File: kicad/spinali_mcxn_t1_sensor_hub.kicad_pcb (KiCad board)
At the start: 4 copper layers, 186 parts, among them J1 5055780421, J2 USB4105-GF-A, J3 CAN0A, J4 CAN0B, J6 CAN1A, J7 CAN1B, J8 DF40TC-50DP-0.4V(51), J9 DF40TC-50DP-0.4V(51), Q1 BUK6D56-60EX, SW1 SW_SPST, U1 LM74700, U10 BMM350, U11 BMP581, U12 TJA1462ATK, U13 TJA1462ATK, U14 SK9822-EC20, U15 TJA1103AHN, U2 NX5P3363UKZ, U3 LM5160DNTJ, U4 NX5P3363UKZ, U5 MIC5504-1.8YMT, U6 MPM3811GG-Z, U7 MCXN947VDFT, U8 PCMF1USB3SZ, U9 ICM-45686, Y1 24MHz, Y2 32.768kHz, Y3 25MHz

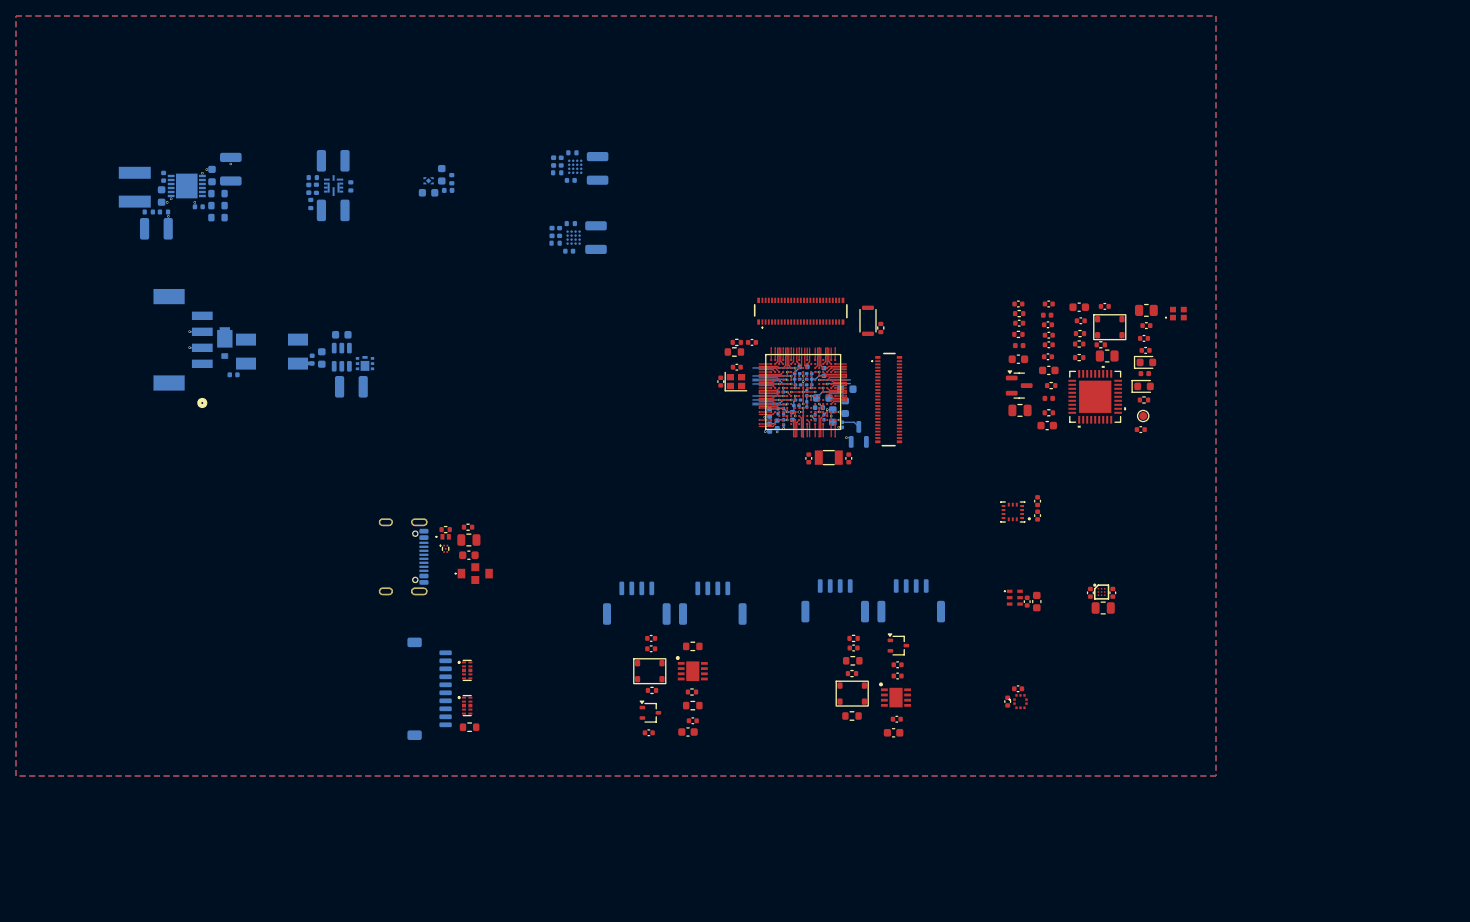
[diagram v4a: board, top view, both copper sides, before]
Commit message: Updated schematic after feedback from Jari
- Finished schematic after feedback from Jari. It is at a finished state, can be reviewed by whole team now.
- Layouted MCXN with decoupling caps.
- Layouted Base100-T1 ethernet phy.
- Layouted the power supply a bit.
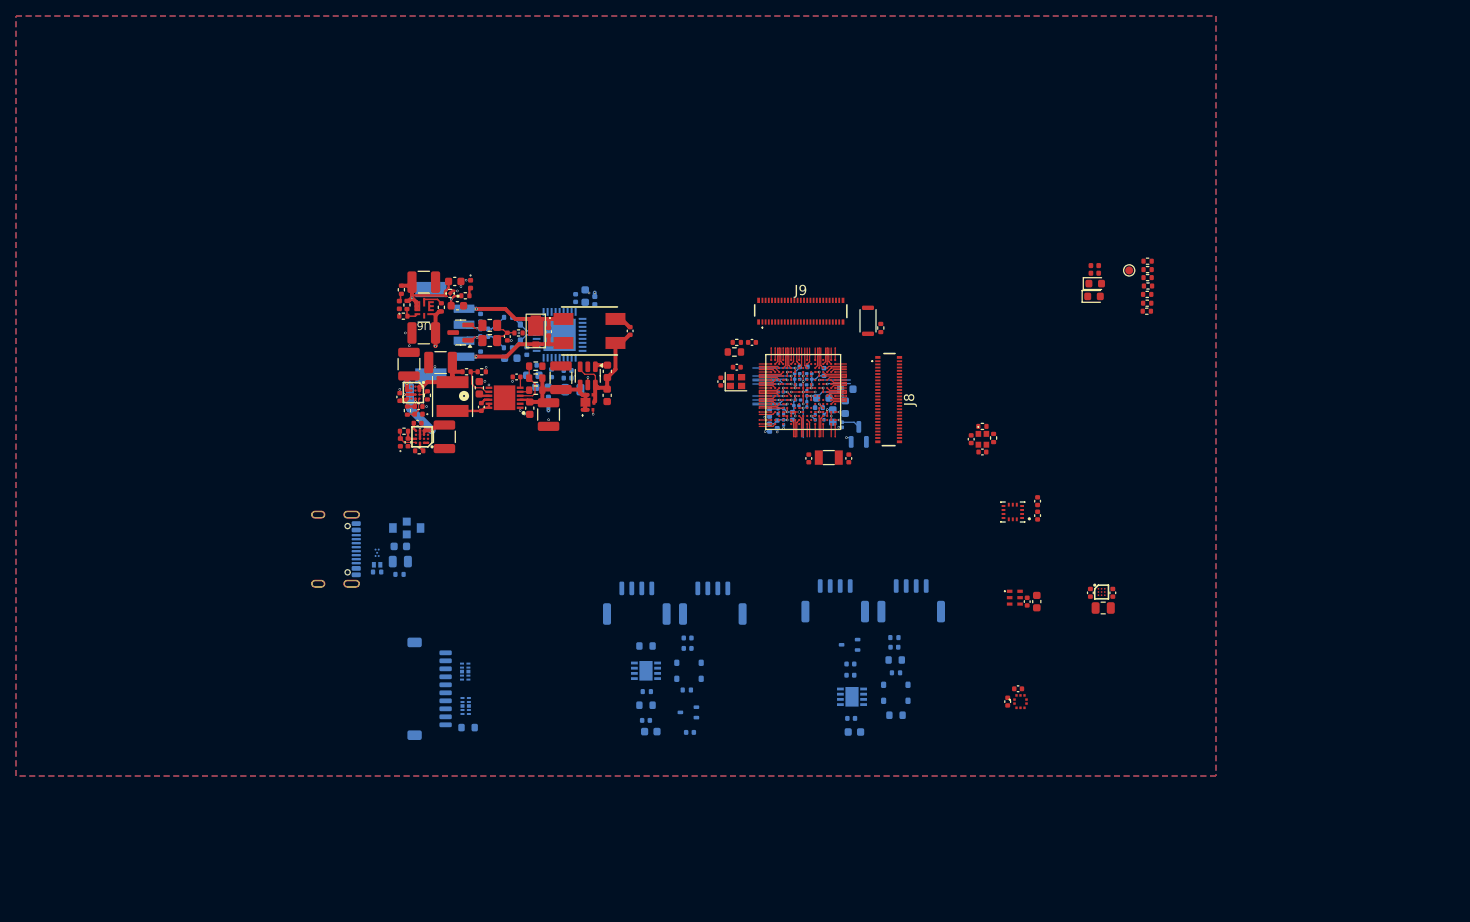
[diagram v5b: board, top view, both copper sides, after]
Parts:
- added R42: 15, Resistor_SMD:R_0402_1005Metric, F.Cu at (155.8, 101.3)
- added R43: 15, Resistor_SMD:R_0402_1005Metric, F.Cu at (157.2, 102.8)
- added R44: 100k 1/10W, Resistor_SMD:R_0402_1005Metric, F.Cu at (97.8, 89.6)
- C1, C10, C11, C12, C13, C14, C15, C16, C17, C18, C19, C2, C20, C21, C3, C4, C5, C6, C7, C8, C9, D2, D3, D4, D5, L1, L2, Q1, R1, R10, R11, R12, R13, R14, R2, R3, R4, R5, R6, R7, R8, R9, U1, U2, U3, U4, U5, U6: moved to F.Cu
- C53, C54, C55, C63, C64, C65, C66, C67, C68, C69, C70, C71, C72, C75, C76, C77, C78, C79, C80, C81, C82, C83, C84, C85, C86, C87, C89, C90, D10, D11, D15, D8, D9, L5, L6, L7, L8, L9, R18, R19, R20, R21, R22, R23, R24, R25, R26, R27, R28, R35, R38, U12, U13, U15, U8: moved to B.Cu
- C91, C92: value 8pF 16V -> 10pF 16V
- D1: value 6DFN62CA-M3/I -> 6DFN56CA-M3/I; moved to F.Cu
- J5: value ~ -> Debug
- J8, J9: value DF40TC-50DP-0.4V(51) -> DF40TC(3.0)-50DP-0.4V(51); footprint Connectors:DF40TC-50DP-0.4V(51) -> Connectors:DF40TC(3.0)-50DP-0.4V(51)
- moved C87 83.1 mm to (93.1, 91.5), turned to 90 degrees
- moved C90 82.8 mm to (93.5, 89.1), turned to 180 degrees
- moved C86 82.5 mm to (93.5, 90.1), turned to 180 degrees
- moved R36 82.1 mm to (94.2, 88.7)
- moved C89 78.0 mm to (93.1, 87.7), turned to 90 degrees
- moved R37 77.2 mm to (94.2, 90.6)
- moved R38 74.2 mm to (96.5, 87.7)
- moved L9 72.2 mm to (98.0, 88.6), turned to 180 degrees
- moved D14 70.1 mm to (90.6, 89.6), turned to 180 degrees
- moved C85 68.8 mm to (99.6, 94.9)
- moved R35 68.1 mm to (96.5, 91.5), turned to 180 degrees
- moved C88 67.6 mm to (96.4, 90.1), turned to -90 degrees
- moved C84 67.6 mm to (96.8, 92.8)
- moved U15 67.4 mm to (103.0, 89.9), turned to 90 degrees
- moved C83 65.3 mm to (98.8, 91.9), turned to 90 degrees
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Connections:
- net /Ethernet PHY/TRX_M renamed /Ethernet PHY/TRX_N
- C1 pad 2: GND -> Net-(C1-Pad2)
- C88 pad 1: GND -> Net-(C88-Pad1)
- C88 pad 2: Net-(C88-Pad2) -> GND
- C89 pad 1: ENET0_TRX_M -> ENET0_TRX_N
- C90 pad 2: ENET0_TRX_M -> ENET0_TRX_N
- C91 pad 1: /Ethernet PHY/ENET0_XTAL_IN -> Net-(C91-Pad1)
- C92 pad 1: /Ethernet PHY/ENET0_XTAL_OUT -> Net-(C92-Pad1)
- D1 pad 1: GND -> Net-(C1-Pad2)
- D14 pad 2: ENET0_TRX_M -> ENET0_TRX_N
- J1 pad 3: ENET0_TRX_M -> ENET0_TRX_N
- J1 pad 4: GND -> Net-(C1-Pad2)
- L1 pad 1: Net-(C1-Pad1) -> Net-(C1-Pad2)
- L1 pad 2: GND -> Net-(C1-Pad1)
- L1 pad 3: GND -> Net-(Q1-S)
- L1 pad 4: Net-(Q1-S) -> GND
- R36 pad 1: ENET0_TRX_P -> ENET0_TRX_N
- R36 pad 2: Net-(C88-Pad2) -> Net-(C88-Pad1)
- R37 pad 1: Net-(C88-Pad2) -> ENET0_TRX_P
- R37 pad 2: ENET0_TRX_M -> Net-(C88-Pad1)
- Y3 pad 1: /Ethernet PHY/ENET0_XTAL_IN -> Net-(C92-Pad1)
- Y3 pad 3: /Ethernet PHY/ENET0_XTAL_OUT -> Net-(C91-Pad1)
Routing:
- net +5V: track 0.00 -> 26.6 mm, vias 0 -> 3
- net +3V3: track 56.2 -> 35.5 mm, vias 8 -> 11
- net +BATT: track 0.00 -> 17.4 mm
- net Net-(Q1-S): track 1.78 -> 16.1 mm
- net Net-(C1-Pad1): track 0.00 -> 14.2 mm, vias 0 -> 1
- net Net-(U4-EN): track 0.00 -> 14.2 mm, vias 0 -> 2
- net Net-(C1-Pad2): track 0.00 -> 14.1 mm, vias 0 -> 1
- net Net-(U7H-VDD_CORE_1): track 17.1 -> 9.46 mm
- net GND: track 18.0 -> 25.1 mm, vias 26 -> 39
- net Net-(Q1-G): track 0.00 -> 6.39 mm, vias 0 -> 2
- net Net-(U3-EN/UVLO): track 0.00 -> 5.67 mm
- net ENET0_TRX_N: track 0.00 -> 5.28 mm, vias 0 -> 1
- net Net-(C9-Pad2): track 0.00 -> 5.22 mm
- net Net-(U3-FB): track 0.00 -> 5.00 mm
- net Net-(C88-Pad1): track 0.00 -> 4.77 mm
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- added copper zone on In3.Cu, net +3V3
- added copper zone on In2.Cu, net GND
- added copper zone on In4.Cu, net GND
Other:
- copper layers 4 -> 6

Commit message: Finished schematic. Completed power and ENET phy layout.
Layouted power supply and ethernet phy around input connector.
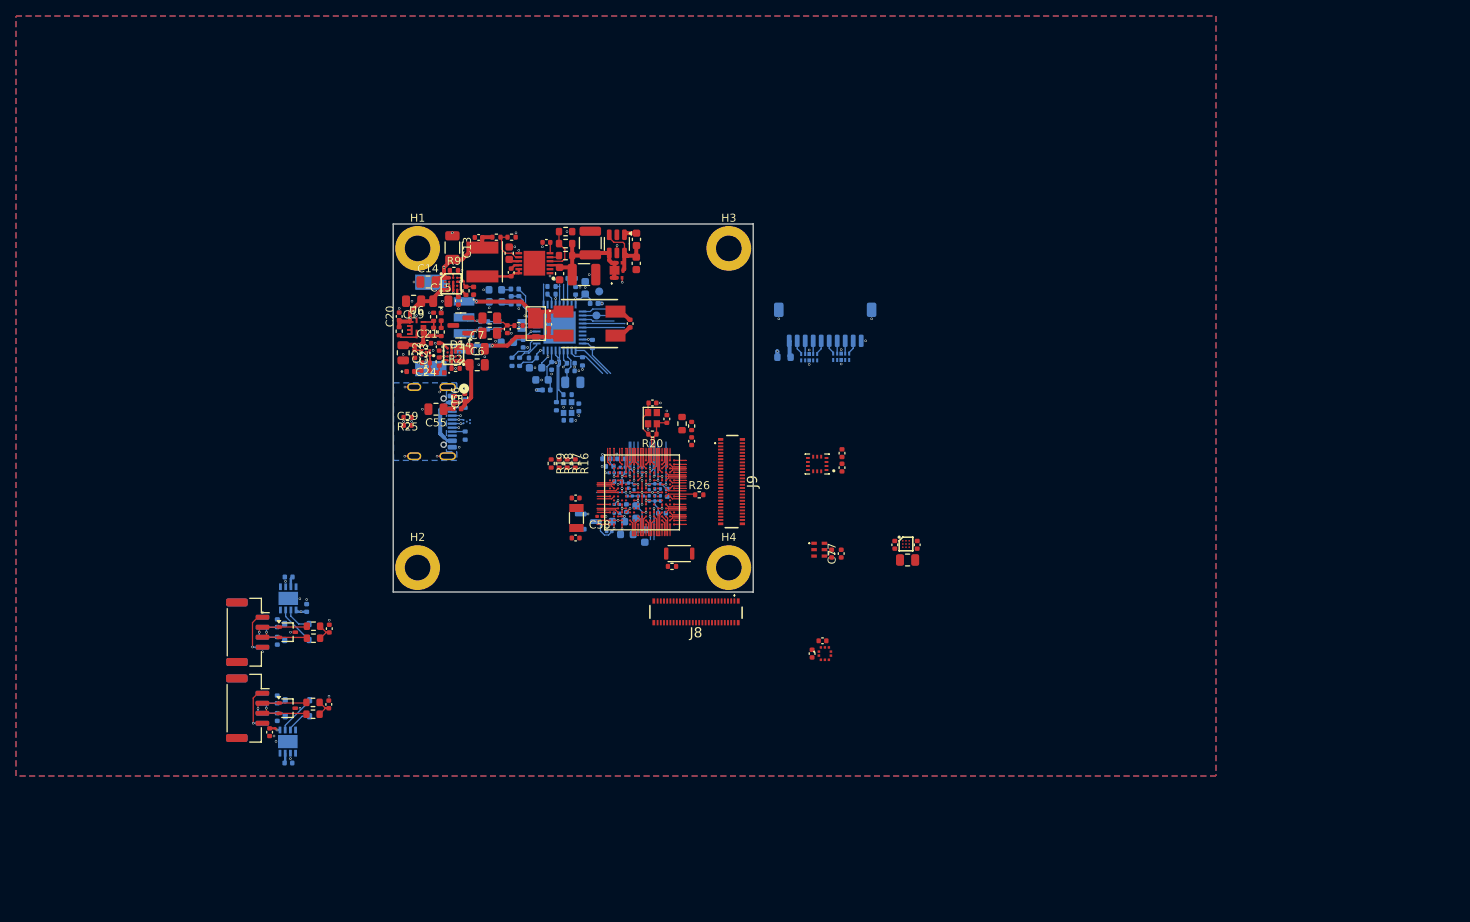
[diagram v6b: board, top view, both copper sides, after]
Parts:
- removed the C12 at (88.1, 93.3)
- removed the C16 at (86.0, 83.3)
- removed the C46 at (137.1, 100.0)
- removed the C53 at (83.8, 114.0)
- removed the C54 at (83.0, 118.2)
- removed the C65 at (139.3, 131.0)
- removed the C67 at (139.3, 132.4)
- removed the C70 at (119.0, 129.1)
- removed the C72 at (119.0, 127.8)
- removed the C87 at (93.1, 91.5)
- removed the C89 at (93.1, 87.7)
- removed the L9 at (98.0, 88.6)
- removed the R14 at (86.4, 97.4)
- removed the R23 at (144.8, 127.7)
- removed the R28 at (113.8, 134.4)
- removed the R35 at (96.5, 91.5)
- removed the R38 at (96.5, 87.7)
- added C13: 22uF 10V, Capacitor_SMD:C_1206_3216Metric, F.Cu at (89.5, 79.0)
- added C19: 10uF 10V, Capacitor_SMD:C_0805_2012Metric, F.Cu at (84.7, 85.7)
- added C20: 100nF 16V, Capacitor_SMD:C_0402_1005Metric, F.Cu at (82.9, 87.5)
- added C21: 100nF 16V, Capacitor_SMD:C_0402_1005Metric, F.Cu at (86.4, 90.9)
- added C22: 10uF 10V, Capacitor_SMD:C_0805_2012Metric, F.Cu at (83.4, 92.1)
- added C49: 10uF 6.3V, Capacitor_SMD:C_0603_1608Metric, B.Cu at (110.3, 113.2)
- added C55: 1uF 50V, Capacitor_SMD:C_0805_2012Metric, F.Cu at (87.5, 99.2)
- added C58: 100nF 10V, Capacitor_SMD:C_0201_0603Metric, F.Cu at (108.0, 112.5)
- added C59: 10nF 16V, Capacitor_SMD:C_0402_1005Metric, F.Cu at (84.0, 101.2)
- added C69: 56pF 10V, Capacitor_SMD:C_0402_1005Metric, B.Cu at (67.7, 137.6)
- added C71: 56pF 10V, Capacitor_SMD:C_0402_1005Metric, B.Cu at (67.7, 135.4)
- added C74: 56pF 10V, Capacitor_SMD:C_0402_1005Metric, B.Cu at (67.7, 128.1)
- added C76: 56pF 10V, Capacitor_SMD:C_0402_1005Metric, B.Cu at (67.7, 125.9)
- added H1: MountingHole, MountingHole:MountingHole_3.2mm_M3_DIN965_Pad, F.Cu at (85.2, 79.0)
- added H2: MountingHole, MountingHole:MountingHole_3.2mm_M3_DIN965_Pad, F.Cu at (85.2, 119.0)
- added H3: MountingHole, MountingHole:MountingHole_3.2mm_M3_DIN965_Pad, F.Cu at (124.1, 79.0)
- added H4: MountingHole, MountingHole:MountingHole_3.2mm_M3_DIN965_Pad, F.Cu at (124.1, 119.0)
- added L10: ACT1210L-201-2P-TL00, Inductors:ACT1210L1012PTL00, B.Cu at (96.7, 88.7)
- added L5: 600 Ohm, Inductor_SMD:L_0402_1005Metric, F.Cu at (90.2, 99.1)
- added R16: 10k, Resistor_SMD:R_0402_1005Metric, F.Cu at (104.9, 105.9)
- added R17: 10k, Resistor_SMD:R_0402_1005Metric, F.Cu at (103.9, 105.9)
- added R18: 10k, Resistor_SMD:R_0402_1005Metric, F.Cu at (102.9, 105.9)
- added R19: 10k, Resistor_SMD:R_0402_1005Metric, F.Cu at (101.9, 105.9)
- added R26: 0R, Resistor_SMD:R_0402_1005Metric, F.Cu at (120.4, 109.8)
- added R36: 10k, Resistor_SMD:R_0402_1005Metric, B.Cu at (97.8, 85.5)
- added R9: 30k 1%, Resistor_SMD:R_0402_1005Metric, F.Cu at (89.7, 81.8)
- added TP2: GND, TestPoint:TestPoint_Pad_D1.0mm, B.Cu at (107.9, 84.4)
- C14, C15: value 47uF 16V -> 10uF 10V; footprint Capacitor_SMD:C_1210_3225Metric -> Capacitor_SMD:C_0805_2012Metric
- C16: renamed from C19; value 22nF 10V -> 22nF 16V
- C23: renamed from C17; footprint Capacitor_SMD:C_0603_1608Metric -> Capacitor_SMD:C_0402_1005Metric
- C24: renamed from C18; footprint Capacitor_SMD:C_0603_1608Metric -> Capacitor_SMD:C_0402_1005Metric
- C56: renamed from C55; footprint Capacitor_SMD:C_0603_1608Metric -> Capacitor_SMD:C_0402_1005Metric; moved to F.Cu
- C6: value 100nF 16V -> 10uF 10V; footprint Capacitor_SMD:C_0402_1005Metric -> Capacitor_SMD:C_0805_2012Metric
- C67: renamed from C63; moved to F.Cu
- C68: renamed from C64; footprint Capacitor_SMD:C_0603_1608Metric -> Capacitor_SMD:C_0402_1005Metric
- C7: value 47uF 16V -> 10uF 16V; footprint Capacitor_SMD:C_1210_3225Metric -> Capacitor_SMD:C_0805_2012Metric
- C70: renamed from C66; moved to F.Cu
- C73: renamed from C69; footprint Capacitor_SMD:C_0603_1608Metric -> Capacitor_SMD:C_0402_1005Metric
- C75: renamed from C71; moved to F.Cu
- C77: renamed from C73; footprint Capacitor_SMD:C_0603_1608Metric -> Capacitor_SMD:C_0402_1005Metric
- C9: value 10nF 16V -> 10nF 25V
- C90: renamed from C91; moved to B.Cu
- C91: renamed from C92; moved to B.Cu
- D10, D11, J4, J7: moved to F.Cu
- D12, D13, R39, TP1, Y3: moved to B.Cu
- D14: value VETH100A203S-G3-18 -> PESD2ETH1G-T
- D7: renamed from D15; moved to F.Cu
- L2: value 33uH 1.3A -> 22uH 1.8A
- R2: value 24k 1% -> 30k 1%
- R20: value 0 -> 1M; moved to F.Cu
- R25: value 0 -> 0R; moved to F.Cu
- R27: renamed from R21; moved to F.Cu
- R28: renamed from R22; moved to F.Cu
- R3: value 100k 75V -> 100k 1% 75V
- R30: renamed from R26; moved to F.Cu
- R31: renamed from R27; moved to F.Cu
- R32: renamed from R29; moved to B.Cu
- R33: renamed from R30; moved to B.Cu
- R34: renamed from R31; moved to B.Cu
- R35: renamed from R32; moved to B.Cu
- R37: renamed from R33; moved to B.Cu
- R38: renamed from R34; moved to B.Cu
- R4: value 68k 75V -> 68k 1% 75V
- R40: renamed from R41; moved to B.Cu
- R41: renamed from R40; moved to B.Cu
- R42: renamed from R43; moved to B.Cu
- R43: renamed from R42; moved to B.Cu
- R5: value 3k3 -> 3k3 1%
- R7: renamed from R11; value 12k 75V -> 12k 1% 75V
- R8: renamed from R12; value 2k2 -> 2k2 1%
- moved J3 84.0 mm to (64.0, 136.5), turned to 90 degrees
- moved R35 79.8 mm to (97.0, 93.2), turned to -90 degrees
- moved R34 79.1 mm to (98.0, 93.2), turned to 90 degrees
- moved D13 75.0 mm to (94.9, 84.2)
- moved L6 74.8 mm to (71.7, 135.5)
- moved D12 74.8 mm to (95.0, 85.7)
- moved J4 74.7 mm to (64.0, 136.5), turned to -90 degrees
- moved R39 74.6 mm to (101.9, 84.8), turned to 180 degrees
- moved R41 74.5 mm to (101.9, 83.8), turned to 180 degrees
- moved R37 73.1 mm to (96.9, 85.5), turned to -90 degrees
- moved R27 73.0 mm to (72.1, 135.8), turned to 0 degrees
- moved R28 72.9 mm to (72.1, 137.3)
- moved C67 72.7 mm to (66.7, 139.5), turned to -90 degrees
- moved R38 72.5 mm to (97.3, 84.1), turned to 180 degrees
- moved R40 72.0 mm to (104.5, 82.8)
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- renumbered C13 to C12, C20 to C17, C21 to C18, C22 to C25, C23 to C26, C24 to C27, C25 to C28, C26 to C29, C27 to C30, C28 to C31, C29 to C32, C30 to C33, C31 to C34, C32 to C35, C33 to C36, C34 to C37, C35 to C38, C36 to C39, C37 to C40, C38 to C41, C39 to C42, C40 to C43, C41 to C44, C42 to C45, C43 to C46, C44 to C47, C45 to C48, C47 to C50, C48 to C51, C49 to C52, C50 to C53, C51 to C54, C52 to C57, C56 to C60, C57 to C61, C58 to C62, C59 to C63, C60 to C64, C61 to C65, C62 to C66, C68 to C72, C74 to C78, C75 to C79, C76 to C80, C77 to C81, C78 to C82, C79 to C83, C80 to C84, C81 to C85, C82 to C86, C83 to C87, C84 to C88, C85 to C89, C86 to C92, C90 to C93, C88 to C94, D5 to D3, D3 to D4, D4 to D5, L5 to L6, L6 to L7, L7 to L8, L8 to L9, R6 to R10, R7 to R11, R8 to R12, R9 to R13, R13 to R14, R16 to R21, R17 to R22, R18 to R23, R19 to R24, R24 to R29, R36 to R44, R37 to R45, R44 to R46, R10 to R6
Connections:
- net P0_18/FC0_P2 renamed P0_18/FC0_P2/IMU_SYNC
- net P0_24/FC1_P0 renamed P0_24/FC1_P0_UART_RXD
- net P0_25/FC1_P1 renamed P0_25/FC1_P1_UART_TXD
- net P3_14/FC8_P0 renamed P3_14/FC8_P0_SPI_SDO
- net P3_15/FC8_P1 renamed P3_15/FC8_P1_SPI_SCK
- net P3_16/FC8_P2 renamed P3_16/FC8_P2_SPI_SDI
- net P3_17/FC8_P3 renamed P3_17/FC8_P3_SPI_PCS0
- net P3_22/FC8_P6 renamed P3_22/FC8_P6_SPI_HREQ
- C14 pad 2: +5V -> Net-(U4-EN)
- C15 pad 1: GND -> +5V
- C15 pad 2: +5V -> GND
- C7 pad 1: GND -> +5V
- C7 pad 2: +5V -> GND
- C84 pad 1: Net-(U15-VDDA_AO) -> /Ethernet PHY/VDDA_AO
- C85 pad 2: Net-(U15-VDDA_AO) -> /Ethernet PHY/VDDA_AO
- C86 pad 2: Net-(U15-VDDA_AO) -> /Ethernet PHY/VDDA_AO
- J2 pad S1: GND -> Net-(J2-SHIELD)
- L9 pad 2: Net-(U15-VDDA_AO) -> /Ethernet PHY/VDDA_AO
- R20 pad 1: Net-(U12-CANH) -> /MCU IO Part 1/XTAL48M
- R20 pad 2: Net-(D10-A1) -> /MCU IO Part 1/EXTAL48M
- R25 pad 1: Net-(U13-CANH) -> GND
- R25 pad 2: Net-(D11-A1) -> Net-(J2-SHIELD)
- R32 pad 1: +3V3 -> VDDIO
- R33 pad 1: +3V3 -> VDDIO
- R34 pad 1: +3V3 -> /Ethernet PHY/VDDA_AO
- R39 pad 1: +3V3 -> VDDIO
- U10 pad A1: unconnected-(U10-INT-PadA1) -> P0_19/BMM350_I2C_INT
- U11 pad 6: GND -> +3V3
- U11 pad 7: unconnected-(U11-INT-Pad7) -> P0_11/BMP581_I2C_INT
- U15 pad 7: Net-(U15-VDDA_AO) -> /Ethernet PHY/VDDA_AO
- U15 pad 9: Net-(U15-VDDA_AO) -> /Ethernet PHY/VDDA_AO
- U7 pad B11: unconnected-(U7A-P0_11/ADC0_B11/CT0_MAT1/FLEXIO0_D3/HSCMP2_OUT-PadB11) -> P0_11/BMP581_I2C_INT
- U7 pad B7: unconnected-(U7A-P0_23/ADC0_A15/CMP2_IN2/EWM0_OUT_b/FC1_P3/CT_INP3/FLEXIO0_D7/WUU0_IN5-PadB7) -> P0_23/FLEXIO0_D7
- U7 pad C9: unconnected-(U7A-P0_19/TSI0_CH14/ADC0_A11/EWM0_OUT_b/FC0_P3/CT0_MAT3/FLEXIO0_D3/HSCMP1_OUT/WUU0_IN3-PadC9) -> P0_19/BMM350_I2C_INT
- U7 pad P3: /MCU IO USB & Power/ANA_0 -> unconnected-(U7G-ANA_0/ADC0_A0-PadP3)
- U7 pad R3: /MCU IO USB & Power/ANA_1 -> unconnected-(U7G-ANA_1/ADC0_B0-PadR3)
- U7 pad T2: /MCU IO USB & Power/ANA_4 -> unconnected-(U7G-ANA_4/ADC1_A0-PadT2)
- U7 pad T3: /MCU IO USB & Power/ANA_5 -> unconnected-(U7G-ANA_5/ADC1_B0-PadT3)
- U7 pad U6: /MCU IO USB & Power/ANA_14 -> unconnected-(U7G-ANA_14/OPAMP0_INN-PadU6)
- U7 pad U8: /MCU IO USB & Power/ANA_18 -> unconnected-(U7G-ANA_18/OPAMP1_INN-PadU8)
- U9 pad 9: unconnected-(U9-INT2/FSYNC/CLKIN-Pad9) -> Net-(U9-INT2/FSYNC/CLKIN)
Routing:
- net VDDIO: track 0.00 -> 25.1 mm, vias 0 -> 5
- net VDDA_TRX: track 0.00 -> 14.3 mm, vias 0 -> 3
- net /Ethernet PHY/VDDA_AO: track 0.00 -> 12.8 mm, vias 0 -> 2
- net Net-(D10-A1): track 0.00 -> 10.9 mm, vias 0 -> 2
- net Net-(D10-A2): track 0.00 -> 10.8 mm, vias 0 -> 1
- net Net-(D11-A2): track 0.00 -> 10.8 mm, vias 0 -> 1
- net Net-(D11-A1): track 0.00 -> 10.6 mm, vias 0 -> 1
- net VBUS: track 4.04 -> 14.5 mm, vias 0 -> 2
- net Net-(D7-K1): track 0.00 -> 10.3 mm, vias 0 -> 1
- net /Ethernet PHY/ENET0_XTAL_IN: track 0.00 -> 6.75 mm
- net /MCU IO Part 1/EXTAL48M: track 2.12 -> 8.52 mm
- net Net-(J2-SHIELD): track 0.00 -> 5.93 mm, vias 0 -> 5
- net /Ethernet PHY/ENET0_XTAL_OUT: track 0.00 -> 5.89 mm
- net Net-(J6-Pad1): track 0.00 -> 5.84 mm, vias 0 -> 1
- net Net-(J3-Pad1): track 0.00 -> 5.70 mm, vias 0 -> 1
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- added copper zone on In2.Cu, net +3V3
- added copper zone on In3.Cu, net GND
- added copper zone on B.Cu, net Net-(J2-SHIELD)
- removed copper zone on In3.Cu, net +3V3
- removed copper zone on In2.Cu, net GND
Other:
- board outline added: 45 x 46 mm

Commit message: Updated layout
Made layout around CANBUS and USB-C.
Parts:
- C67: moved to B.Cu
- C72: moved to F.Cu
- moved C68 45.1 mm to (95.2, 106.7), turned to 180 degrees
- moved C67 42.3 mm to (97.5, 110.5), turned to 90 degrees
- moved U12 40.9 mm to (95.3, 109.3), turned to -90 degrees
- moved C69 35.0 mm to (94.3, 115.0), turned to 0 degrees
- moved L6 34.6 mm to (97.0, 112.0)
- moved J3 34.2 mm to (93.2, 118.8), turned to 180 degrees
- moved J4 34.2 mm to (93.2, 118.8), turned to 0 degrees
- moved R28 32.1 mm to (94.2, 114.0), turned to -90 degrees
- moved C71 31.9 mm to (92.1, 115.0), turned to 0 degrees
- moved D10 30.9 mm to (90.3, 114.2), turned to 180 degrees
- moved C70 30.6 mm to (93.0, 112.0), turned to 0 degrees
- moved R27 30.0 mm to (92.7, 114.0), turned to 90 degrees
- moved C73 27.3 mm to (92.2, 105.5), turned to 0 degrees
- moved R31 27.1 mm to (90.8, 108.1), turned to -90 degrees
- moved C74 26.9 mm to (89.0, 111.8)
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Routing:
- net /Ethernet PHY/VDDA_AO: track 12.8 -> 17.4 mm, vias 2 -> 3
- net /MCU IO Part 2/P5_0/EXTAL32K: track 1.60 -> 6.04 mm
- net /MCU IO Part 2/P5_1/XTAL32K: track 1.60 -> 6.00 mm
- net Net-(C90-Pad1): track 0.00 -> 3.70 mm
- net Net-(U12-CANL): track 4.99 -> 2.09 mm
- net Net-(D10-A2): track 10.8 -> 13.4 mm
- net Net-(D10-A1): track 10.9 -> 8.87 mm, vias 2 -> 1
- net Net-(C91-Pad1): track 0.00 -> 1.87 mm
- net /Ethernet PHY/ENET0_XTAL_IN: track 6.75 -> 4.90 mm
- net Net-(D11-A1): track 10.6 -> 9.19 mm
- net Net-(U13-CANL): track 3.46 -> 2.11 mm
- net Net-(D11-A2): track 10.8 -> 9.75 mm
- net Net-(C1-Pad1): track 14.2 -> 15.2 mm
- net Net-(U13-CANH): track 4.97 -> 3.97 mm
- net Net-(U12-CANH): track 3.26 -> 4.07 mm
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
